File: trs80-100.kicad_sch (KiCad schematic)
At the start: 197 parts, among them CN2 A-7224, CN3 TCS-4480, CN4 TCS-4490, CN6 RS232C, J1 Adapter Jack CN9, K1 Key_Board, M15 40H244, M21 40H244, M23 40H244, M27 4011, M28 4013, M30 TL064, M33 40H157, M34 4584, M35 4584, SW3 SLB-22BP-03, SW4 Reset Switch, SW5 SSP32201, T10 2SC2603, T11 2SC2603, T13 2SC2603, T14 2SC2603(E), T15 2SC2603(E), T16 2SC2603(E), T17 2SC2603(E), T18 2SC2603, T19 2SA1115, T20 2SC2603, T21 2SC2603(E), T22 2SC2603(E), T25 2SC2603, T27 2SC2603, T28 2SA1115, T6 2SC2603, T9 2SC2603

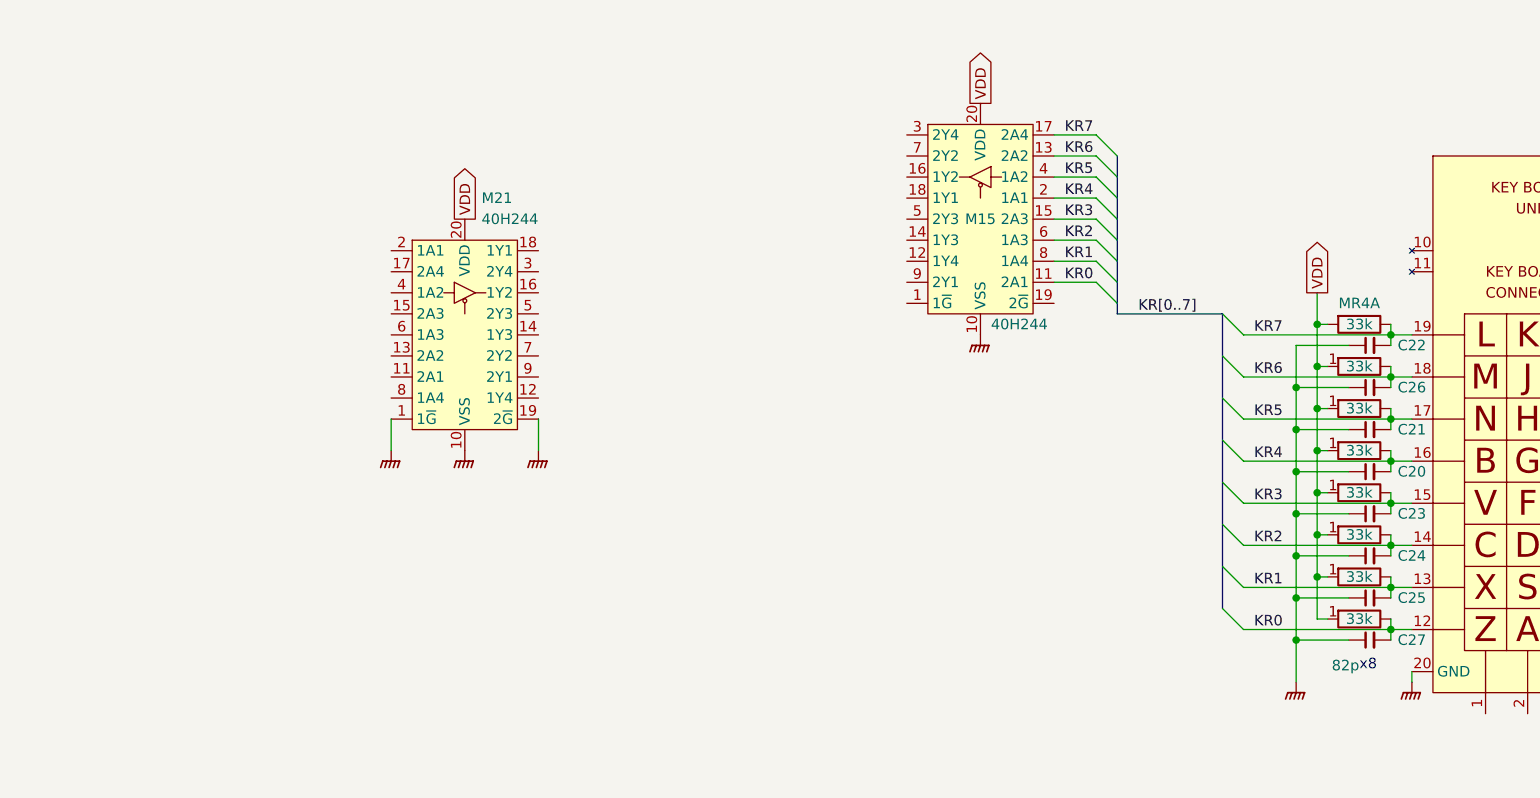
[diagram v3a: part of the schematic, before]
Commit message: Resistor network: make resistors slimmer to fit between pins.
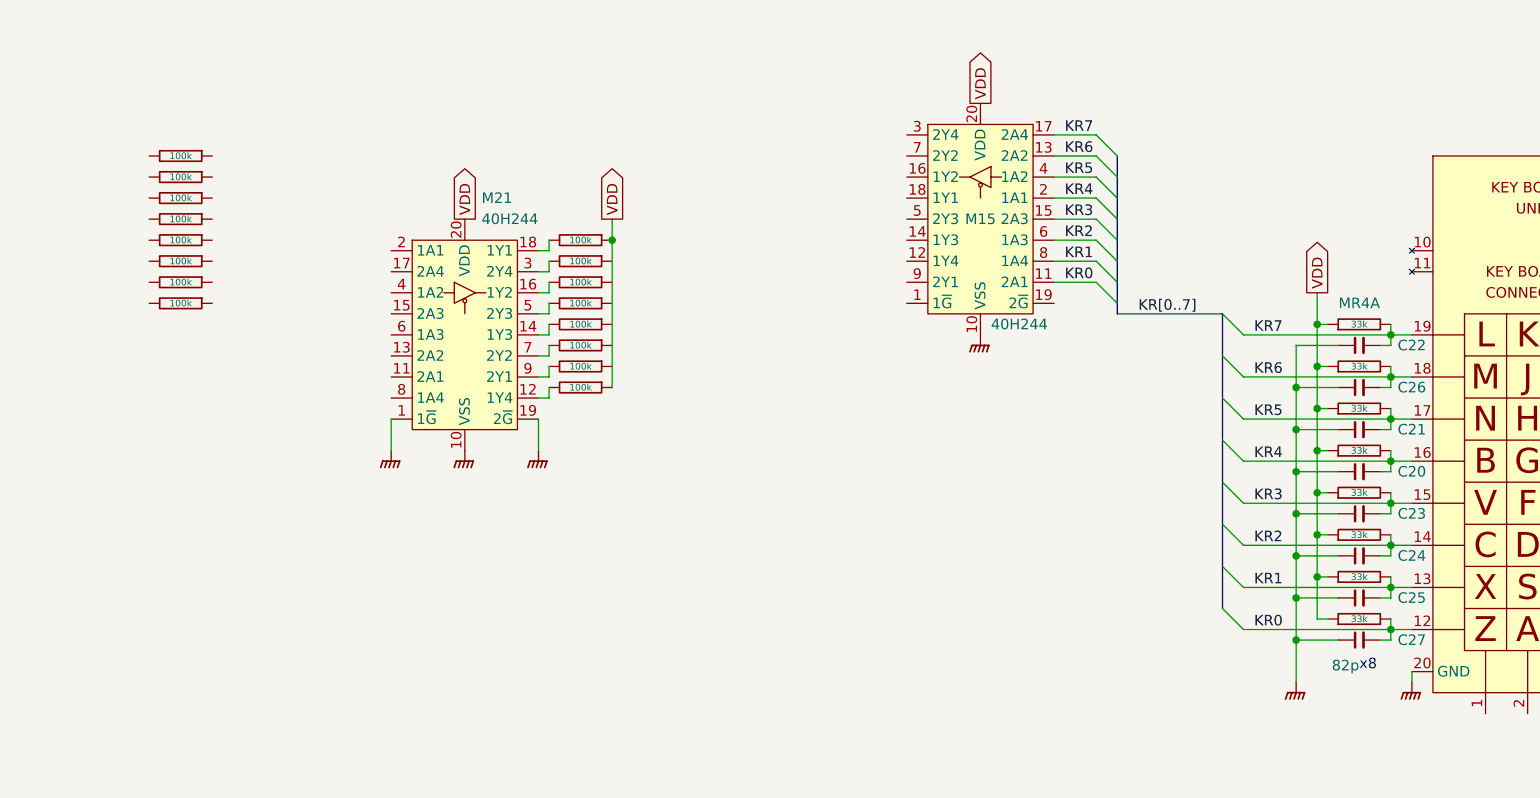
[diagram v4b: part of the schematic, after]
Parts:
- added MR7, MR? (x8): 100k, Resistor_THT:R_Array_SIP9, symbol trs80-100:R_Network
- MR4: symbol Device:R_Network08_Split -> trs80-100:R_Network
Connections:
- net VDD: now also MR7.1 (R1.1)
- net at M21.12 (1Y4): now also MR7.9 (R8.2)
- net at M21.14 (1Y3): now also MR7.6 (R5.2)
- net at M21.16 (1Y2): now also MR7.4 (R3.2)
- net at M21.18 (1Y1): now also MR7.2 (R1.2)
- net at M21.3 (2Y4): now also MR7.3 (R2.2)
- net at M21.5 (2Y3): now also MR7.5 (R4.2)
- net at M21.7 (2Y2): now also MR7.7 (R6.2)
- net at M21.9 (2Y1): now also MR7.8 (R7.2)
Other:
- moved on the sheet: C20, C21, C22, C23, C24, C25, C26, C27

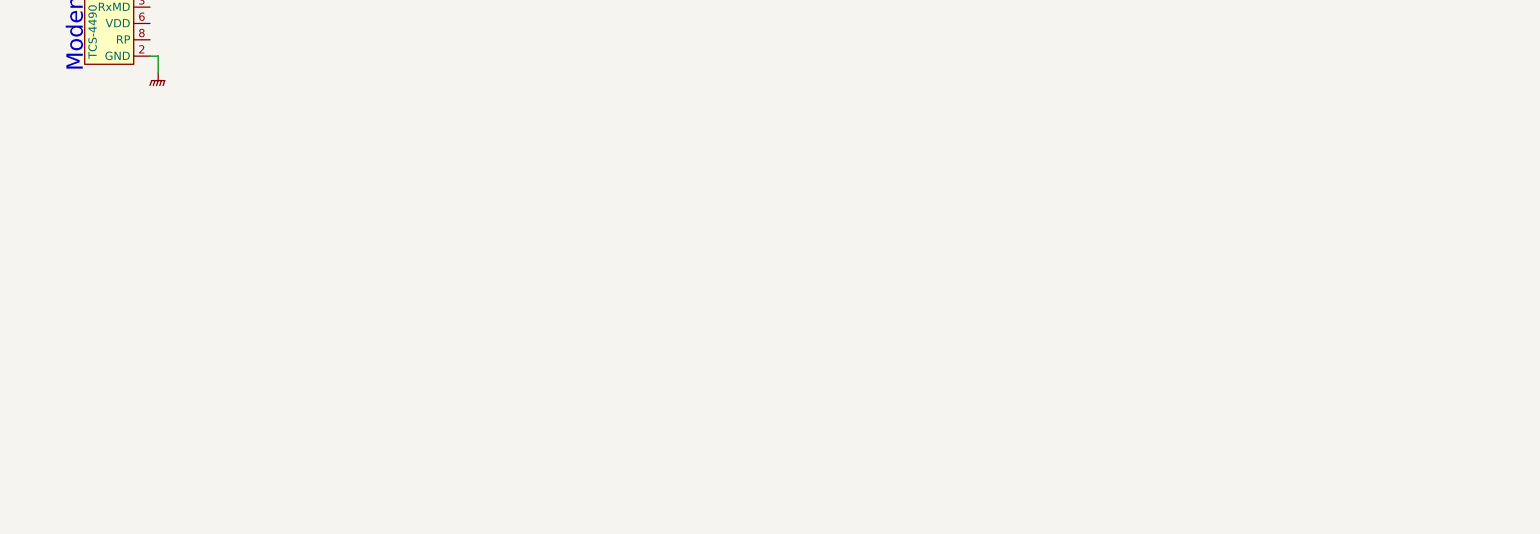
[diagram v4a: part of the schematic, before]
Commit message: Filter section for modem.
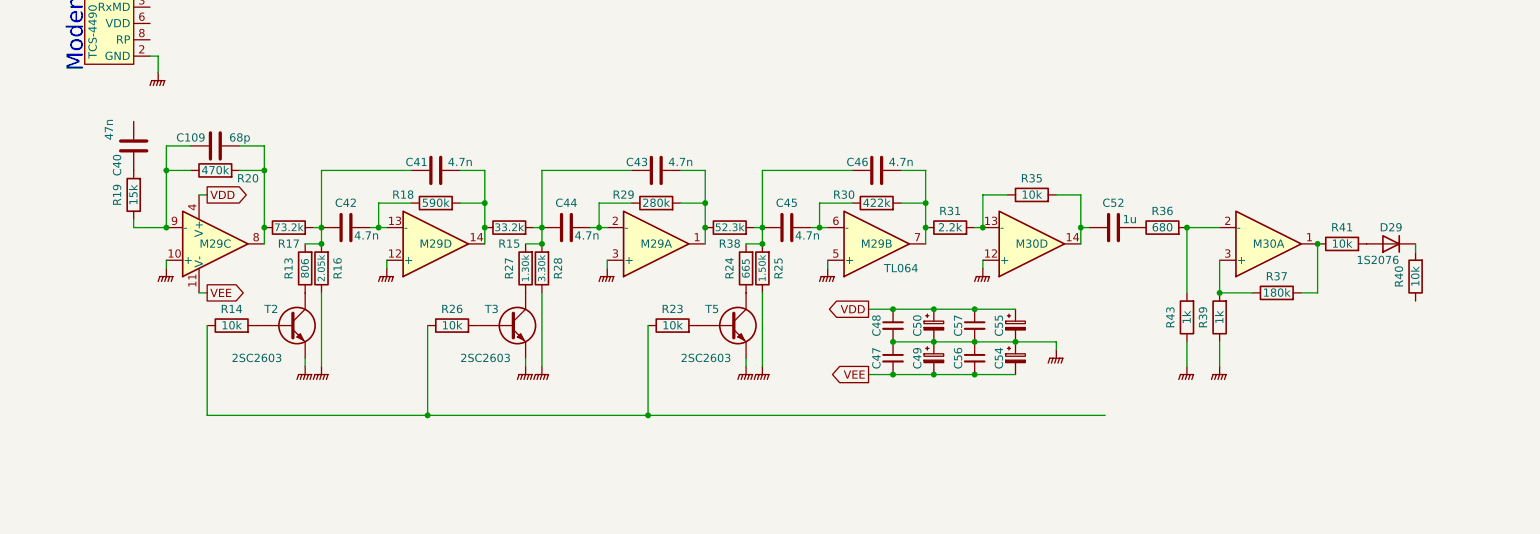
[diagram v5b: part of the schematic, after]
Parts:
- added C109: 68p, symbol Device:C
- added C40: 47n, symbol Device:C
- added C41, C42, C43, C44, C45, C46: 4.7n, symbol Device:C
- added C47, C48, C56, C57: 100n, symbol Device:C_Small
- added C49, C50, C54, C55: 1u, symbol Device:C_Polarized_Small
- added C52: 1u, symbol Device:C
- added D29: 1S2076, symbol Device:D
- added M29: TL064, symbol Amplifier_Operational:TL064
- added unit 4 of M30
- added unit 1 of M30
- added R13: 806, symbol Device:R
- added R14, R23, R26, R35, R40, R41: 10k, symbol Device:R
- added R15: 33.2k, symbol Device:R
- added R16: 2.05k, symbol Device:R
- added R17: 73.2k, symbol Device:R
- added R18: 590k, symbol Device:R
- added R19: 15k, symbol Device:R
- added R20: 470k, symbol Device:R
- added R24: 665, symbol Device:R
- added R25: 1.50k, symbol Device:R
- added R27: 1.30k, symbol Device:R
- added R28: 3.30k, symbol Device:R
- added R29: 280k, symbol Device:R
- added R30: 422k, symbol Device:R
- added R31: 2.2k, symbol Device:R
- added R36: 680, symbol Device:R
- added R37: 180k, symbol Device:R
- added R38: 52.3k, symbol Device:R
- added R39, R43: 1k, symbol Device:R
- added T2, T3, T5: 2SC2603, Package_TO_SOT_THT:TO-92_Inline, symbol Transistor_BJT:2N3904
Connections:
- net GNDPWR: now also C47.1, C48.2, C49.1, C50.2, C54.1, C55.2, C56.1, C57.2, M29.10 (+), M29.12 (+), M29.3 (+), M29.5 (+), M30.12 (+), R16.1, R25.1, R28.1, R39.1, R43.1, T2.1 (E), T3.1 (E), T5.1 (E)
- net VDD: now also C48.1, C50.1, C55.1, C57.1, M29.4 (V+)
- net VEE: now also C47.2, C49.2, C54.2, C56.2, M29.11 (V-)
- new net: C45.1, C46.1, R24.2, R25.2, R38.2
- new net: C41.1, C42.1, R13.2, R16.2, R17.2
- new net: C42.2, M29.13 (-), R18.1
- new net: C46.2, M29.7, R30.2, R31.1
- new net: M30.13 (-), R31.2, R35.1
- new net: C109.1, M29.9 (-), R19.1, R20.1
- new net: C109.2, M29.8, R17.1, R20.2
- new net: R24.1, T5.3 (C)
- new net: R14.2, T2.2 (B)
- new net: R13.1, T2.3 (C)
- new net: C41.2, M29.14, R15.1, R18.2
- new net: C52.2, R36.1
- new net: M30.2 (-), R36.2, R43.2
- new net: C43.1, C44.1, R15.2, R27.2, R28.2
- new net: C43.2, M29.1, R29.2, R38.1
- new net: C44.2, M29.2 (-), R29.1
- new net: C40.1, R19.2
- new net: M30.1, R37.2, R41.1
- new net: D29.2 (A), R41.2
- new net: R26.2, T3.2 (B)
- new net: R27.1, T3.3 (C)
- new net: C45.2, M29.6 (-), R30.1
- new net: M30.3 (+), R37.1, R39.2
- new net: D29.1 (K), R40.2
- new net: R14.1, R23.1, R26.1
- new net: R23.2, T5.2 (B)
- new net: C52.1, M30.14, R35.2

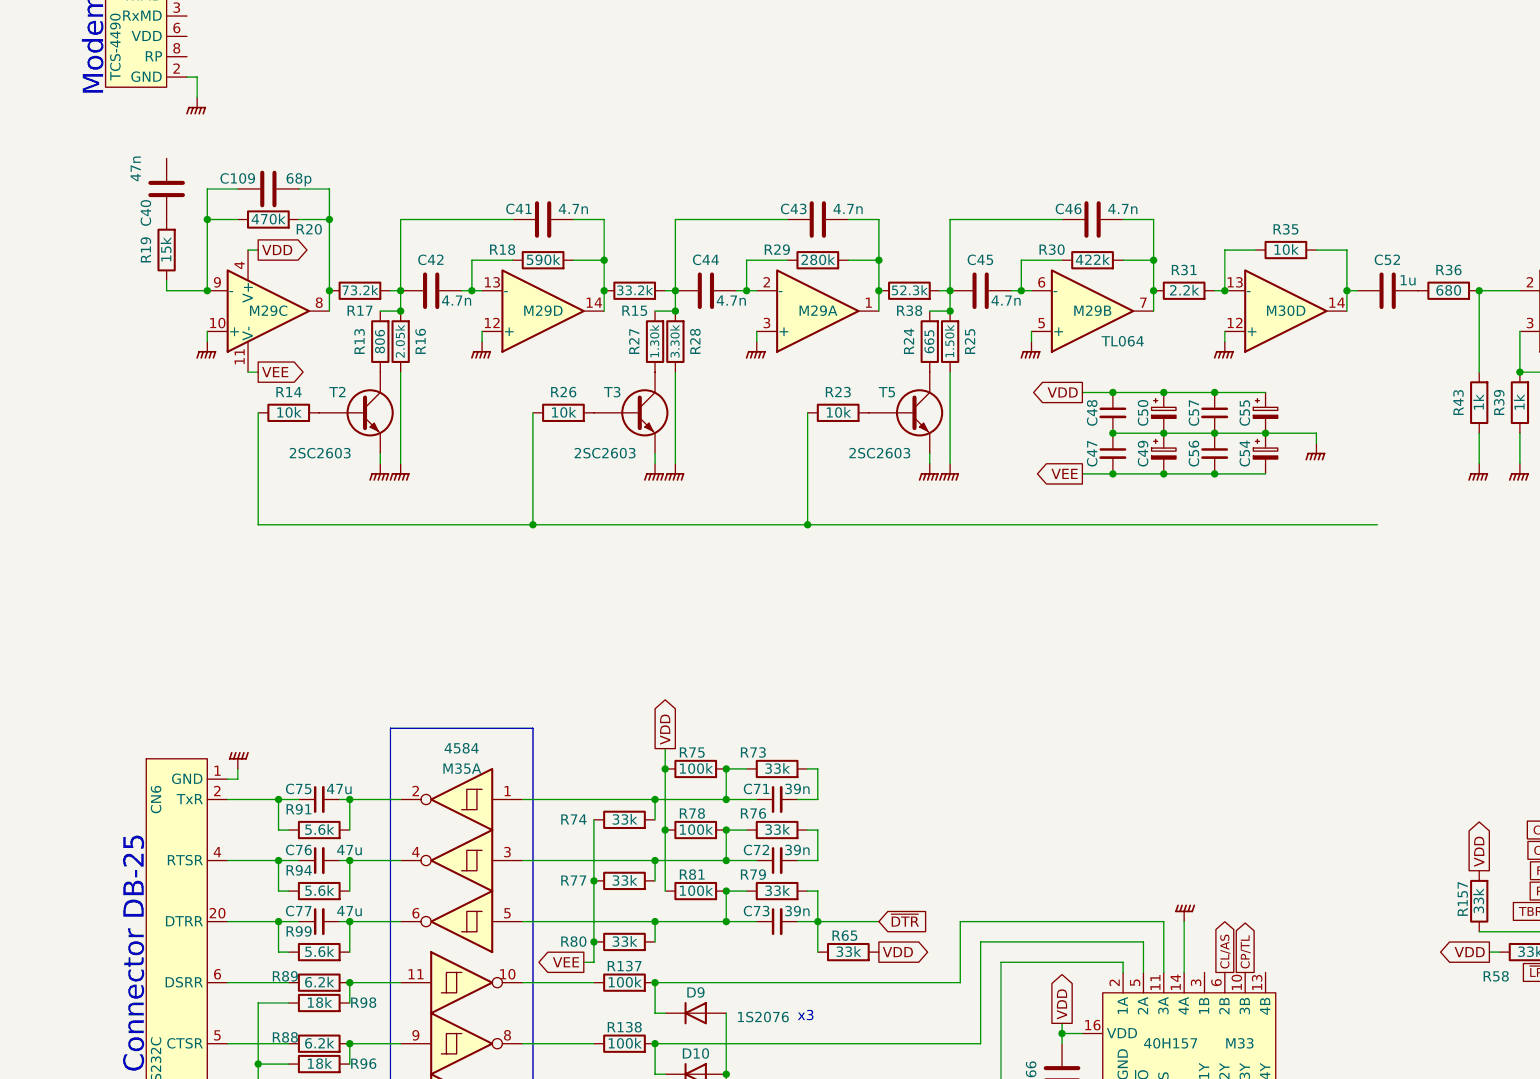
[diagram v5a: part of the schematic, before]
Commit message: Add bipolar capacitors used in RS232 and Modem interface.
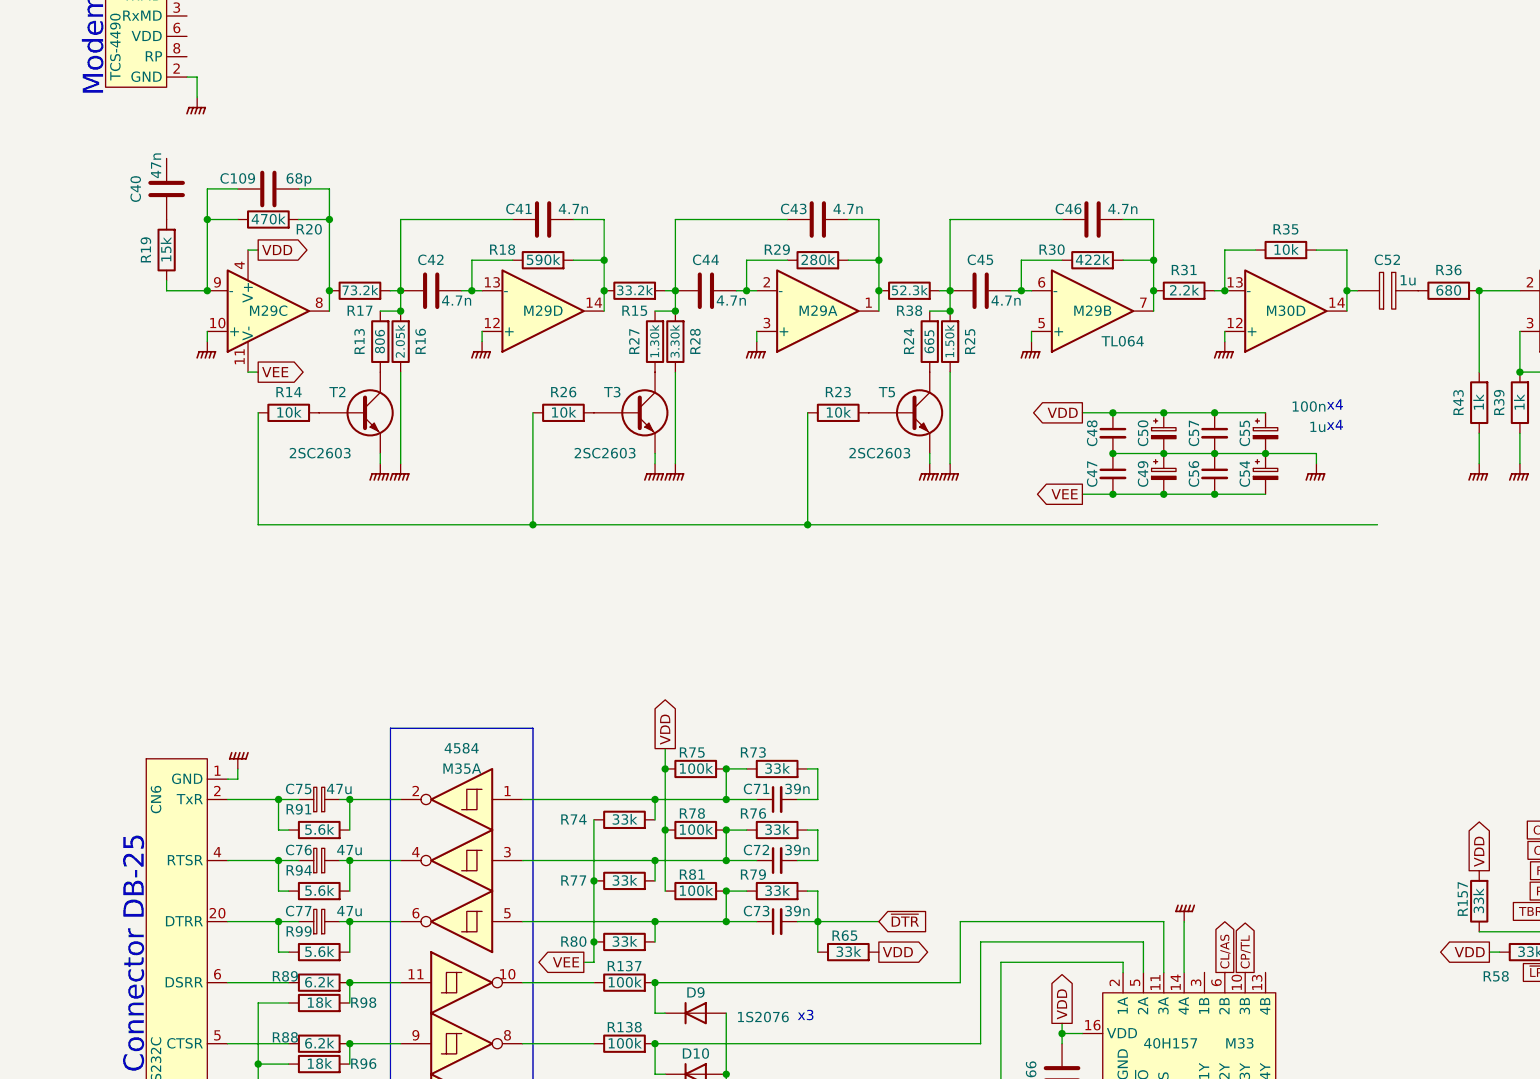
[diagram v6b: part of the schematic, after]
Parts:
- C52: symbol Device:C -> trs80-100:C_Bipolar
- C75, C76, C77: symbol Device:C_Small -> trs80-100:C_Bipolar_Small
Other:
- moved on the sheet: C47, C48, C49, C50, C54, C55, C56, C57
